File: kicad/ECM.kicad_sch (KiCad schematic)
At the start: 100 parts, among them J1 Bus_PCI_Express_x1, J2 Conn_01x04_Pin, J6 USB_C_Receptacle_USB2.0_16P, Q1 AO3400A, Q2 AO3400A, Q3 AO3400A, SW1 SW_DPST_x2, SW2 SW_DPST_x2, SW3 SW_DPDT_x2, U1 MCP25625T-E/ML, U10 MAX31855KASA+T, U11 SY8388ARHC, U2 RP2040, U3 ADS8688IDBTR, U4 W25Q128JVP, U5 TPS22976DPUR, U6 GAQY252G3S, U7 MAX31855KASA+T, U8 MAX31855KASA+T, U9 MAX31855KASA+T, X1 ABM8-272-T3, Y1 X322516MLB4SI

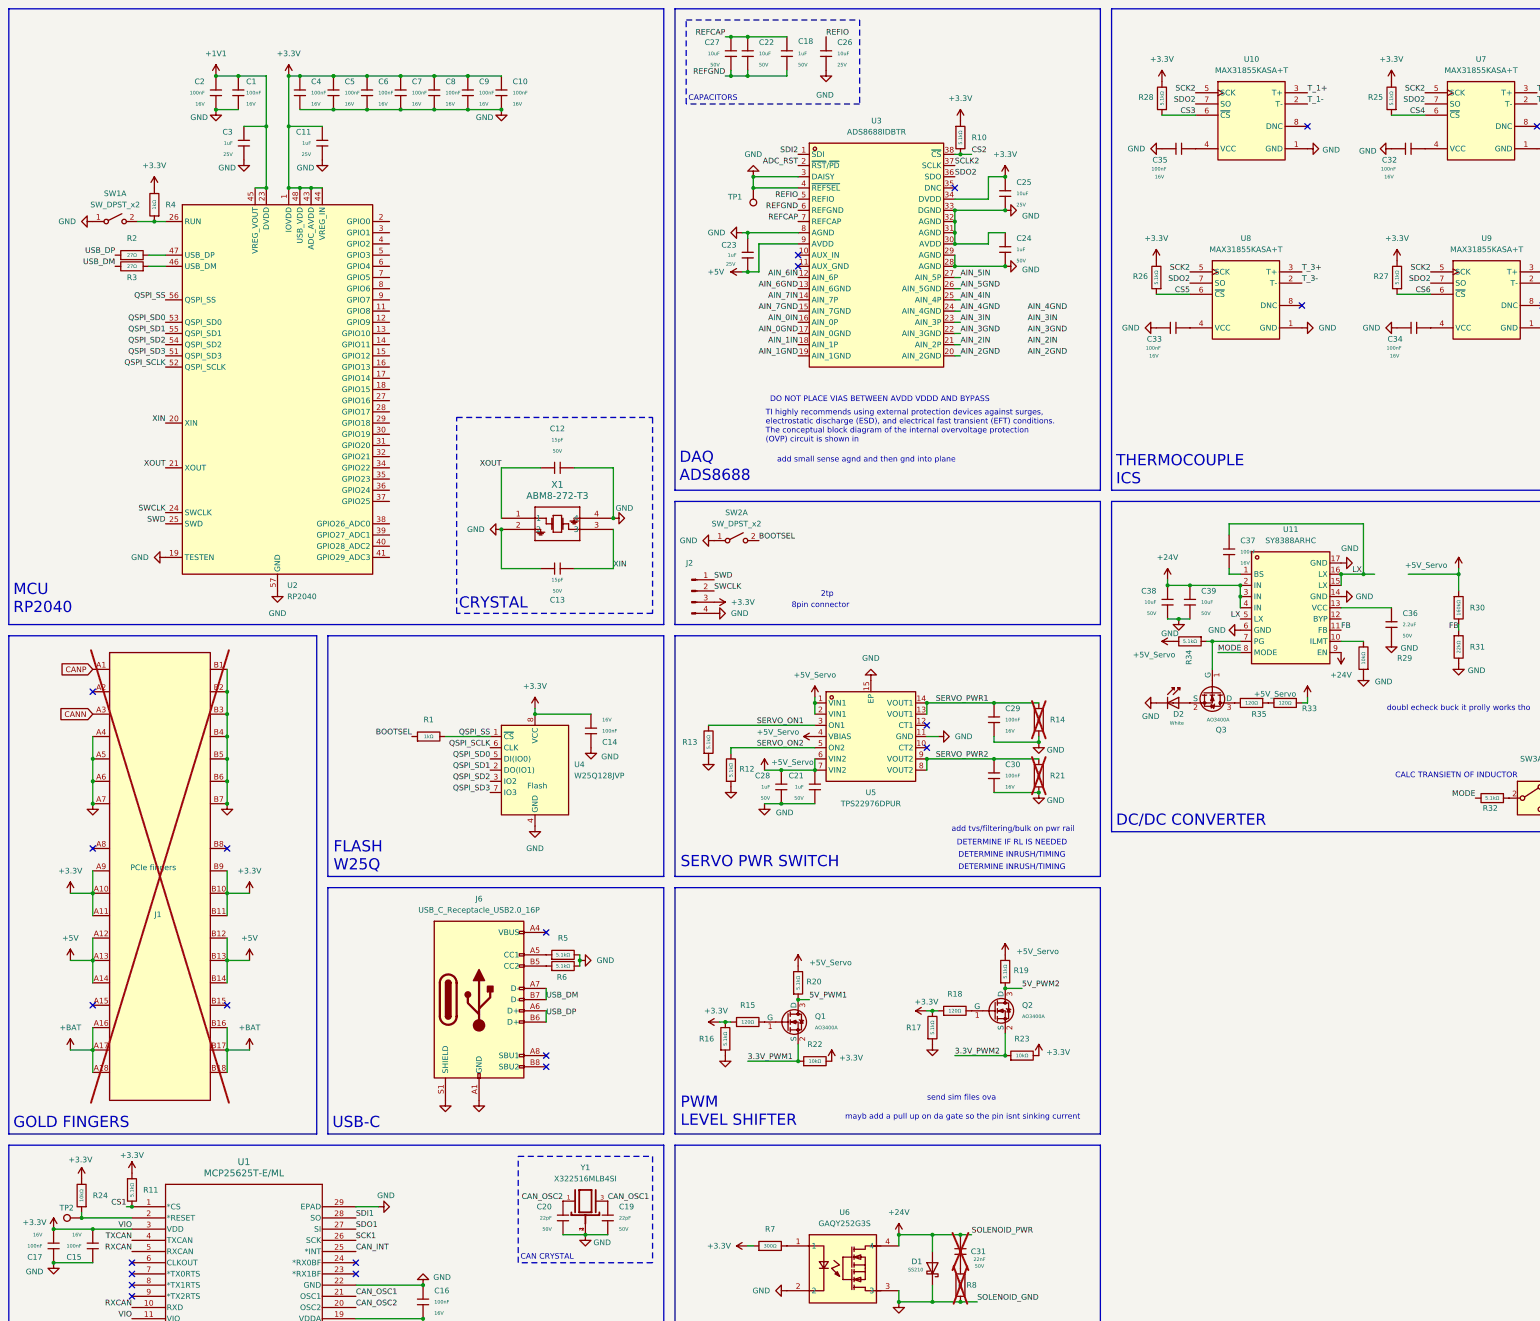
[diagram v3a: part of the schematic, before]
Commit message: Preliminary PCB Layout on most ICs, carved out analog, power and digital regions.
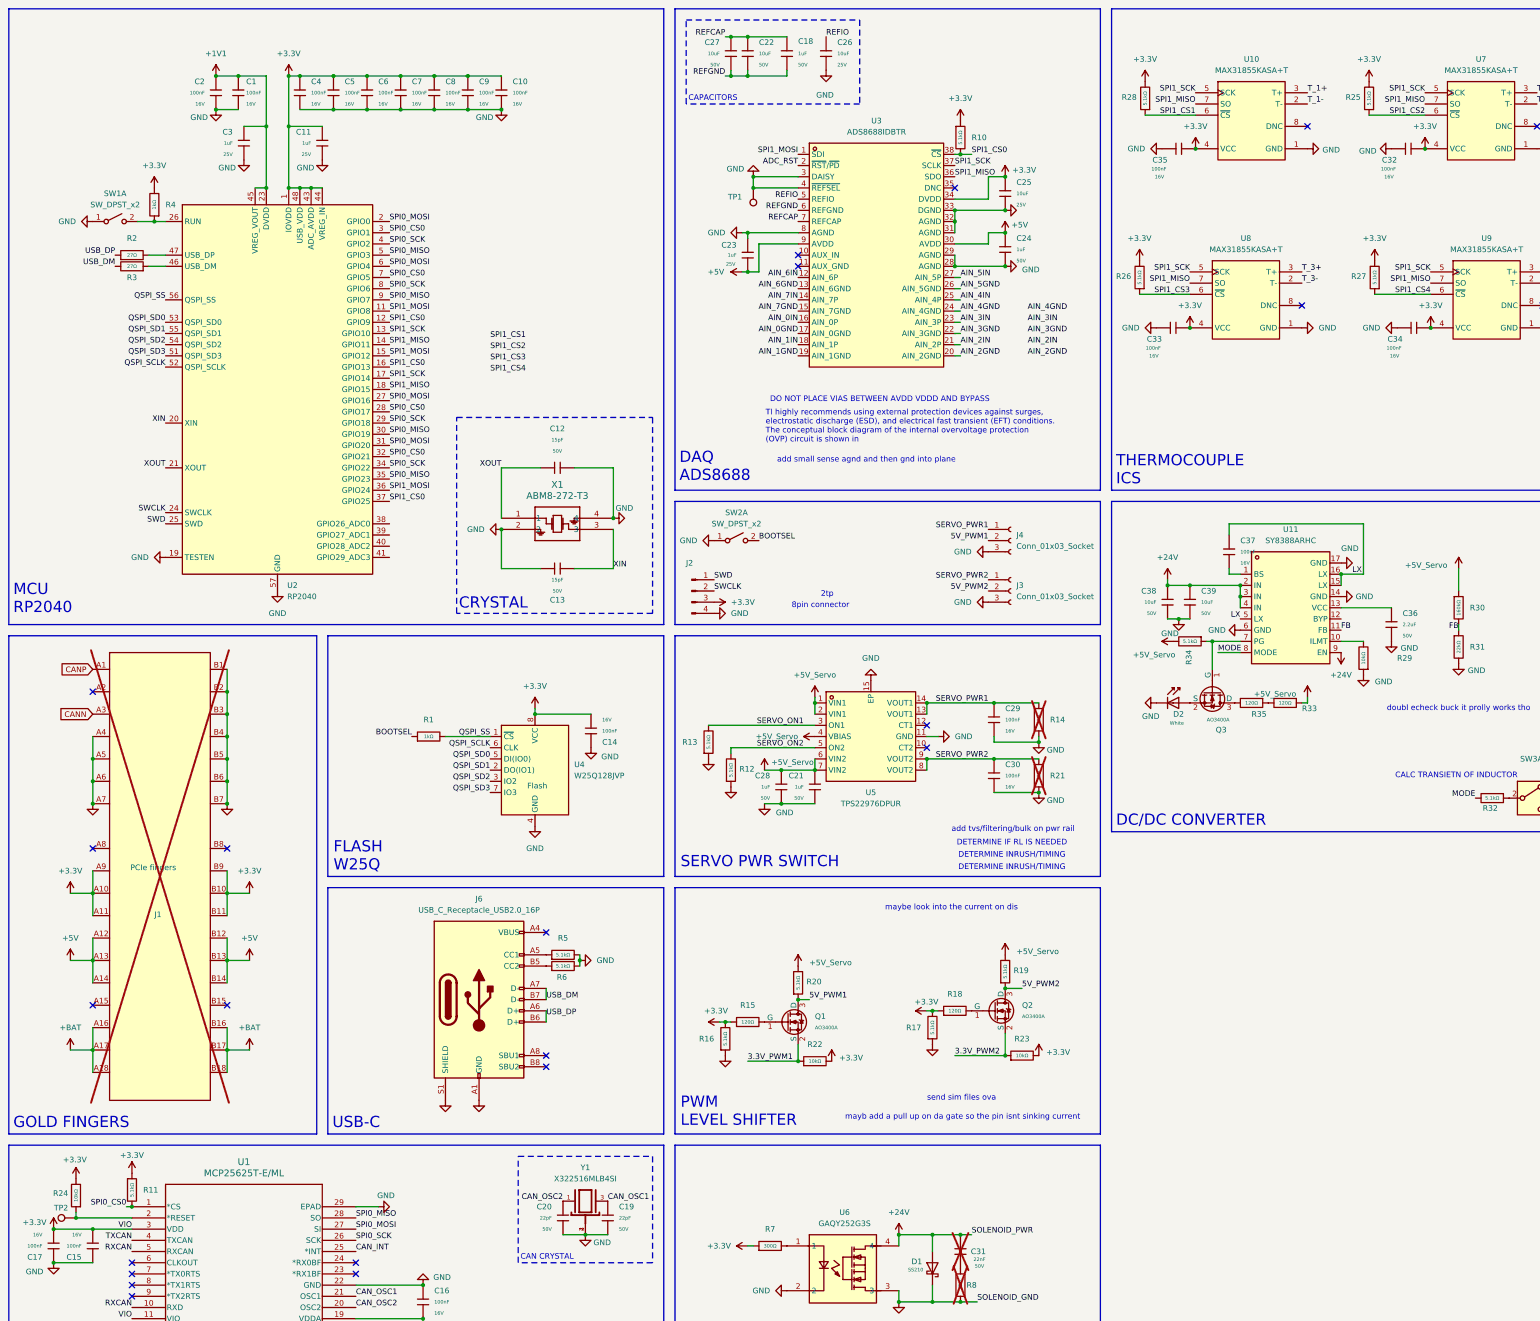
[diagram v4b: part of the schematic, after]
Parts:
- added J3, J4: Conn_01x03_Socket, symbol Connector:Conn_01x03_Socket
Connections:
- net CS1 is gone; now on net SPI0_CS0: R11.2, U1.1 (*CS)
- net CS2 is gone; now on net SPI1_CS0: R10.2, U3.38 (~{CS})
- net SCK1 is gone; now on net SPI0_SCK: U1.26 (SCK)
- net SCK2 is gone; now on net SPI1_SCK: U10.5 (SCK), U7.5 (SCK), U8.5 (SCK), U9.5 (SCK)
- net SCLK2 is gone; now on net SPI1_SCK: U3.37 (SCLK)
- net SDI1 is gone; now on net SPI0_MISO: U1.28 (SO)
- net SDI2 is gone; now on net SPI1_MOSI: U3.1 (SDI)
- net SDO1 is gone; now on net SPI0_MOSI: U1.27 (SI)
- net SDO2 is gone; now on net SPI1_MISO: U10.7 (SO), U3.36 (SDO), U7.7 (SO), U8.7 (SO), U9.7 (SO)
- net +3.3V: now also C32.2, C33.2, C34.2, C35.2, U10.4 (VCC), U7.4 (VCC), U8.4 (VCC), U9.4 (VCC)
- net +5V: now also C24.1, U3.30 (AVDD)
- net 5V_PWM1: now also J4.2 (Pin_2)
- net 5V_PWM2: now also J3.2 (Pin_2)
- net GND: now also J3.3 (Pin_3), J4.3 (Pin_3); no longer C24.1, U3.30 (AVDD)
- net SERVO_PWR1: now also J4.1 (Pin_1)
- net SERVO_PWR2: now also J3.1 (Pin_1)
- net SPI1_MOSI: now reaches U2.11 (GPIO8)
- net SPI1_MOSI: now also U2.15 (GPIO12), U2.36 (GPIO24)
- net SPI1_CS0: now reaches U2.12 (GPIO9)
- net SPI1_CS0: now also U2.16 (GPIO13), U2.37 (GPIO25)
- net SPI1_SCK: now reaches U2.13 (GPIO10)
- net SPI1_SCK: now also U2.17 (GPIO14)
- net SPI1_MISO: now reaches U2.14 (GPIO11)
- net SPI1_MISO: now also U2.18 (GPIO15)
- net SPI0_MOSI: now reaches U2.2 (GPIO0)
- net SPI0_MOSI: now also U2.27 (GPIO16), U2.31 (GPIO20), U2.6 (GPIO4)
- net SPI0_CS0: now reaches U2.28 (GPIO17)
- net SPI0_CS0: now also U2.3 (GPIO1), U2.32 (GPIO21), U2.7 (GPIO5)
- net SPI0_SCK: now reaches U2.29 (GPIO18)
- net SPI0_SCK: now also U2.34 (GPIO22), U2.4 (GPIO2), U2.8 (GPIO6)
- net SPI0_MISO: now reaches U2.30 (GPIO19)
- net SPI0_MISO: now also U2.35 (GPIO23), U2.5 (GPIO3), U2.9 (GPIO7)
- net CS3 renamed SPI1_CS1
- net CS4 renamed SPI1_CS2
- net CS5 renamed SPI1_CS3
- net CS6 renamed SPI1_CS4
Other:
- note added: "maybe look into the current on dis"
- moved on the sheet: R24, R25, R26, R27, R28, TP2

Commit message: More progress on layout
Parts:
- removed C31: 22nF, PCM_JLCPCB:C_0603, symbol PCM_JLCPCB-Capacitors:0603,22nF
- removed R8: 27Ω, PCM_JLCPCB:R_0603, symbol PCM_JLCPCB-Resistors:0603,27Ω
- added C40, C41, C42: 10uF, PCM_JLCPCB:C_0805, symbol PCM_JLCPCB-Capacitors:0805,10uF,(2)
- added C43: 220pF, PCM_JLCPCB:C_0402, symbol PCM_JLCPCB-Capacitors:0402,220pF
- added R36: 160kΩ, PCM_JLCPCB:R_0603, symbol PCM_JLCPCB-Resistors:0603,160kΩ
- added R37: 1kΩ, PCM_JLCPCB:R_0603, symbol PCM_JLCPCB-Resistors:0603,1kΩ
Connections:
- net CANN is gone; now on net CANL: J1.A3 (+12V)
- net CANP is gone; now on net CANH: J1.A1 (~{PRSNT1})
- net +24V: now also R36.2; no longer U11.9 (EN)
- net +5V_Servo: now also C40.1, C41.1, C42.1, C43.1
- net FB: now also R37.2
- net GND: now also C40.2, C41.2, C42.2
- net SPI0_CS0: now also R10.2, U3.38 (~{CS}); no longer R11.2, U1.1 (*CS)
- net SPI0_MISO: now also U10.7 (SO), U3.36 (SDO), U7.7 (SO), U8.7 (SO), U9.7 (SO); no longer U1.28 (SO)
- net SPI0_MOSI: now also U3.1 (SDI); no longer U1.27 (SI)
- net SPI0_SCK: now also U10.5 (SCK), U3.37 (SCLK), U7.5 (SCK), U8.5 (SCK), U9.5 (SCK); no longer U1.26 (SCK)
- net SPI1_CS0: now also R11.2, U1.1 (*CS); no longer R10.2, U3.38 (~{CS})
- net SPI1_MISO: now also U1.28 (SO); no longer U10.7 (SO), U3.36 (SDO), U7.7 (SO), U8.7 (SO), U9.7 (SO)
- net SPI1_MOSI: now also U1.27 (SI); no longer U3.1 (SDI)
- net SPI1_SCK: now also U1.26 (SCK); no longer U10.5 (SCK), U3.37 (SCLK), U7.5 (SCK), U8.5 (SCK), U9.5 (SCK)
- net USB_DM: no longer R3.2
- net USB_DP: no longer J6.A6 (D+), J6.B6 (D+)
- net SPI1_CS1 renamed SPI0_CS1
- net SPI1_CS2 renamed SPI0_CS2
- net SPI1_CS3 renamed SPI0_CS3
- net SPI1_CS4 renamed SPI0_CS34
- new net: R36.1, U11.9 (EN)
- new net: C43.2, R37.1
- new net USB_DN: J6.A6 (D+), J6.B6 (D+), R3.2
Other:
- note added: "(0.432 * 8) = 3.456 W"
- note added: "(5V * 2W)*2 = 20 W"
- note added: "18 W"
- note added: "8A(max) targeting 5 A at 93%"
- note added: "FIGURE OUT DISSISPATION"
- note added: "[(5*(25-5))/(24*600*10^3*(0.4*5))] = 3.3uH = 4.7uH saturation of (1.3*5.4A) = 7A"
- note added: "triple check wiring on can shit makes no sense"
- note removed: "CALC TRANSIETN OF INDUCTOR"
- moved on the sheet: C36, R30, R31
